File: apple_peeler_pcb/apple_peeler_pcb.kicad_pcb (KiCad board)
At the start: 2 copper layers, 130 parts, among them J1 BM03B-SRSS-TB, J2 BM03B-SRSS-TB, J3 HYC10-HDMIA19-600B, J4 HYC10-HDMIA19-600B, J5 USB_C_Receptacle_USB2.0_16P, Q1 2N7002, Q10 2N7002, Q11 2N7002, Q12 2N7002, Q13 2N7002, Q14 AO3401A, Q15 2N7002, Q16 AO3401A, Q17 2N7002, Q18 2N7002, Q2 2N7002, Q3 2N7002, Q4 2N7002, Q5 2N7002, Q6 2N7002, Q7 2N7002, Q8 2N7002, Q9 2N7002, SW1 SPST BTN, SW2 SPST BTN, SW3 SPST BTN, U1 W25Q16JVSS, U2 RP2040, U3 4066, U4 TPS562242, Y1 12MHz

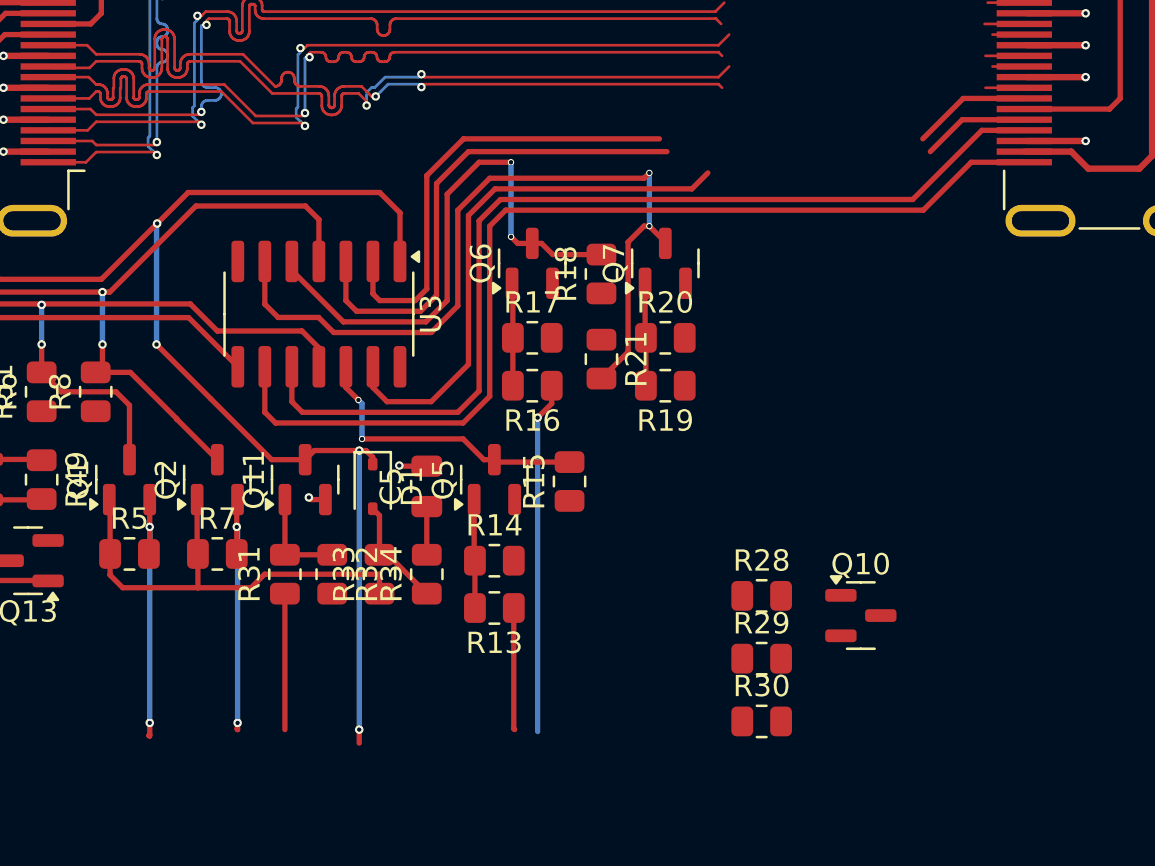
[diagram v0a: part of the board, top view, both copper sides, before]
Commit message: passthrough switch level shifters
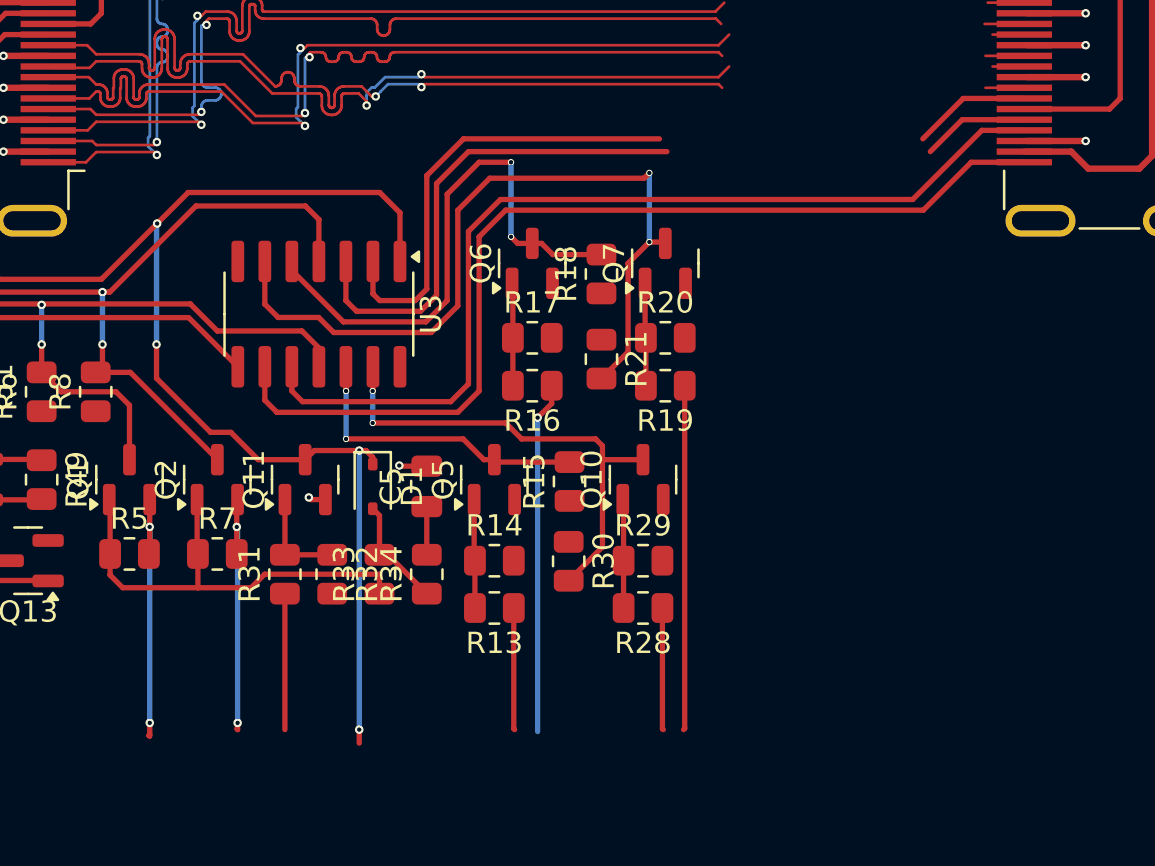
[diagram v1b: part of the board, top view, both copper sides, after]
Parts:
- moved Q10 12.1 mm to (191.5, 125.4), turned to 90 degrees
- moved R30 11.8 mm to (188.0, 129.2), turned to -90 degrees
- moved R29 7.23 mm to (191.5, 129.2)
- moved R28 5.60 mm to (191.5, 131.4), turned to 180 degrees
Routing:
- net /HDMI passthrough/HPD_ARC_BRIDGE: track 0.00 -> 16.2 mm
- net /HDMI passthrough/CEC_BRIDGE: track 0.00 -> 5.73 mm
- net Net-(Q10-G): track 0.00 -> 5.11 mm
- net /HDMI passthrough/Pullup level shifter3/OUT_5V: track 25.5 -> 22.8 mm, vias 0 -> 2
- net /HDMI passthrough/Bidir level shifter2/L_5V: track 46.4 -> 45.2 mm
- net /HDMI passthrough/HDMI connectors/HPD_SINK: track 47.8 -> 46.6 mm
- net /HDMI passthrough/CEC interface/CEC_LINE: track 70.0 -> 70.9 mm

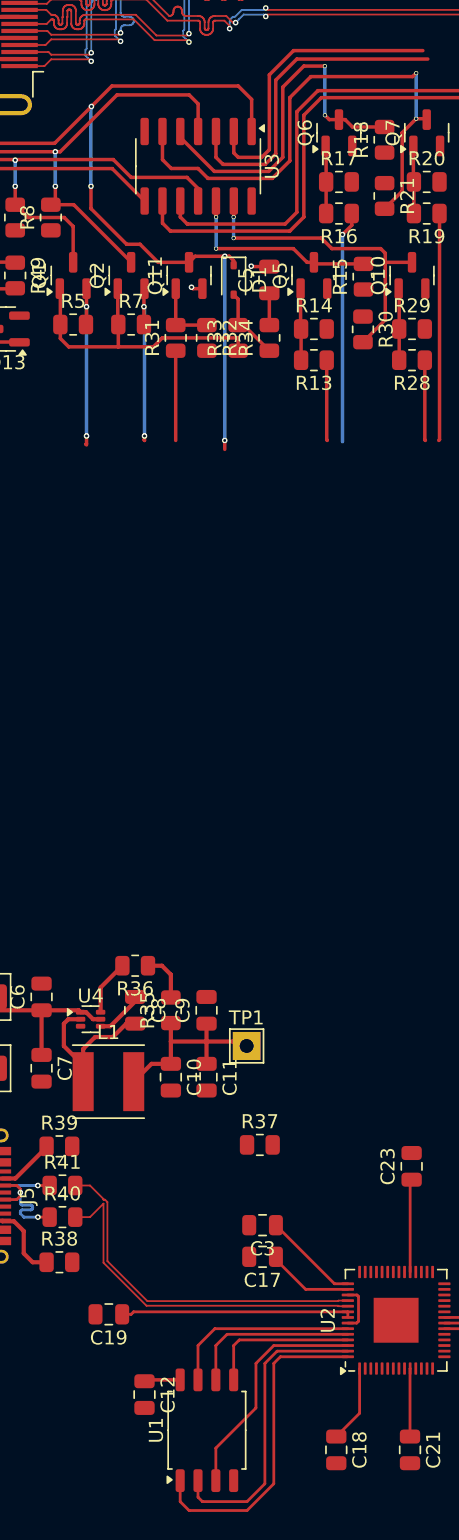
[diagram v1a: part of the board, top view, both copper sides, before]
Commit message: make space for bypass cap near switch chip
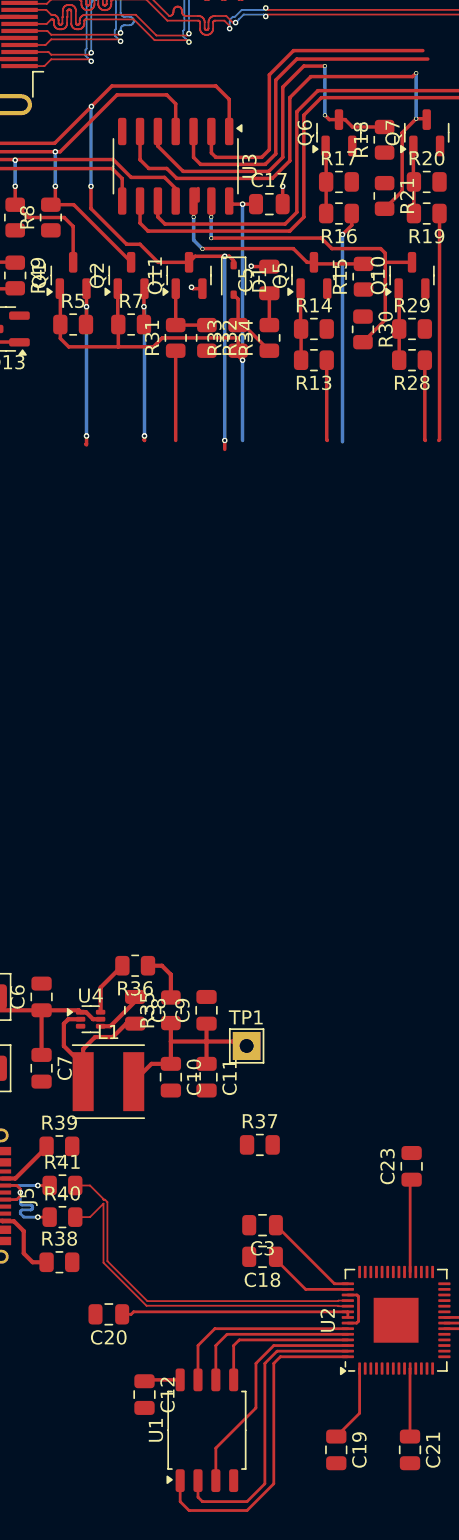
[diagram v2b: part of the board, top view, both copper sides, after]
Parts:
- added C17: 2.2μF, Capacitor_SMD:C_0805_2012Metric, F.Cu at (181.3, 120.3)
- moved U3 1.60 mm to (174.6, 117.6)
- renumbered C17 to C18, C18 to C19, C19 to C20
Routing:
- net +3.3V: track 88.7 -> 108.3 mm, vias 0 -> 2
- net /HDMI passthrough/Bidir level shifter/L_5V: track 46.1 -> 43.6 mm
- net /HDMI passthrough/HDMI connectors/HPD_SINK: track 46.6 -> 48.2 mm
- net /HDMI passthrough/CEC interface/CEC_LINE: track 70.9 -> 69.3 mm
- net /HDMI passthrough/Bidir level shifter2/L_5V: track 45.2 -> 46.8 mm
- net /HDMI passthrough/CEC interface1/CEC_LINE: track 26.9 -> 28.5 mm
- net /HDMI passthrough/Pullup level shifter2/OUT_5V: track 37.7 -> 39.3 mm
- net /HDMI passthrough/Bidir level shifter3/L_5V: track 28.4 -> 30.0 mm
- net /HDMI passthrough/Bidir level shifter1/L_5V: track 46.9 -> 45.3 mm
- net /HDMI passthrough/Pullup level shifter3/OUT_5V: track 22.8 -> 24.4 mm
- net /HDMI passthrough/Pullup level shifter1/OUT_5V: track 25.9 -> 27.4 mm
- net GND: track 29.7 -> 30.9 mm, vias 14 -> 15
- net /HDMI passthrough/Pullup level shifter/OUT_5V: track 14.3 -> 15.4 mm
- net /HDMI passthrough/HDMI connectors/HPD_SRC: track 45.3 -> 44.7 mm

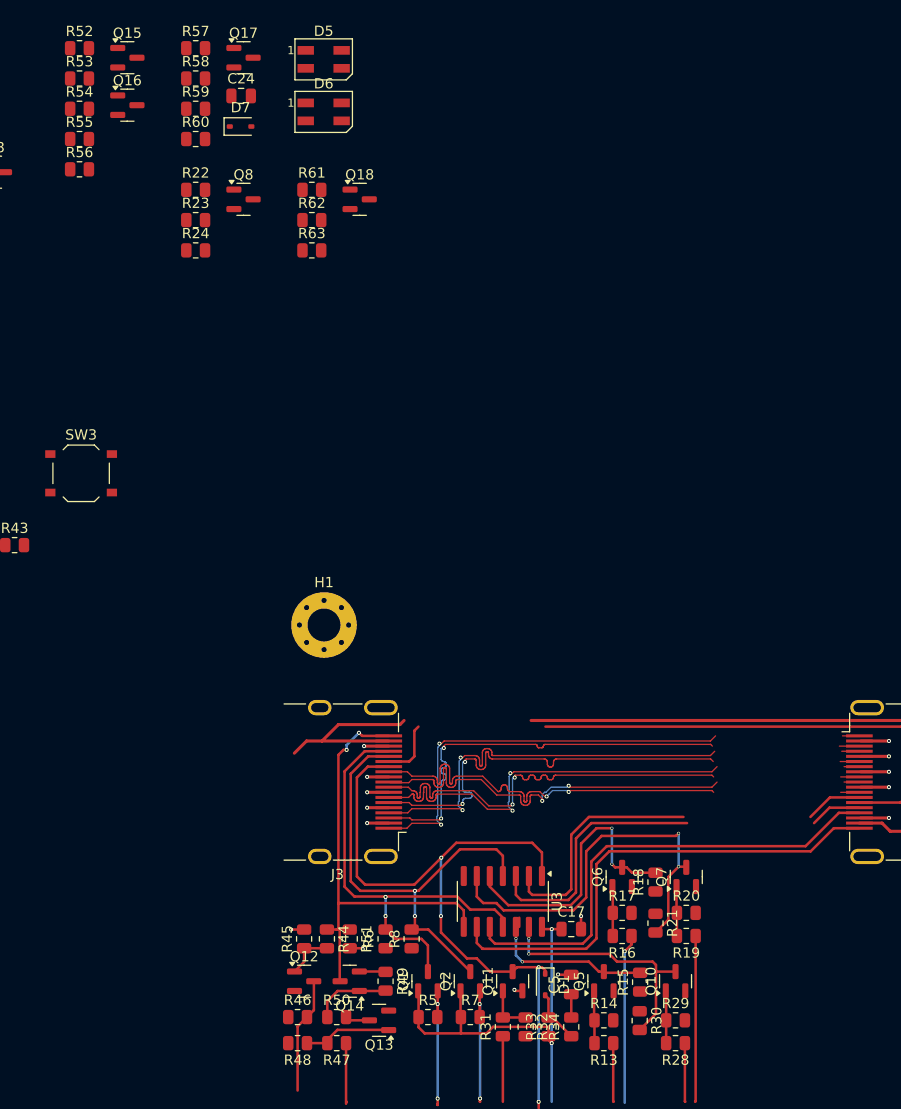
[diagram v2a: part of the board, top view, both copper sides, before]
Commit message: route HPD B
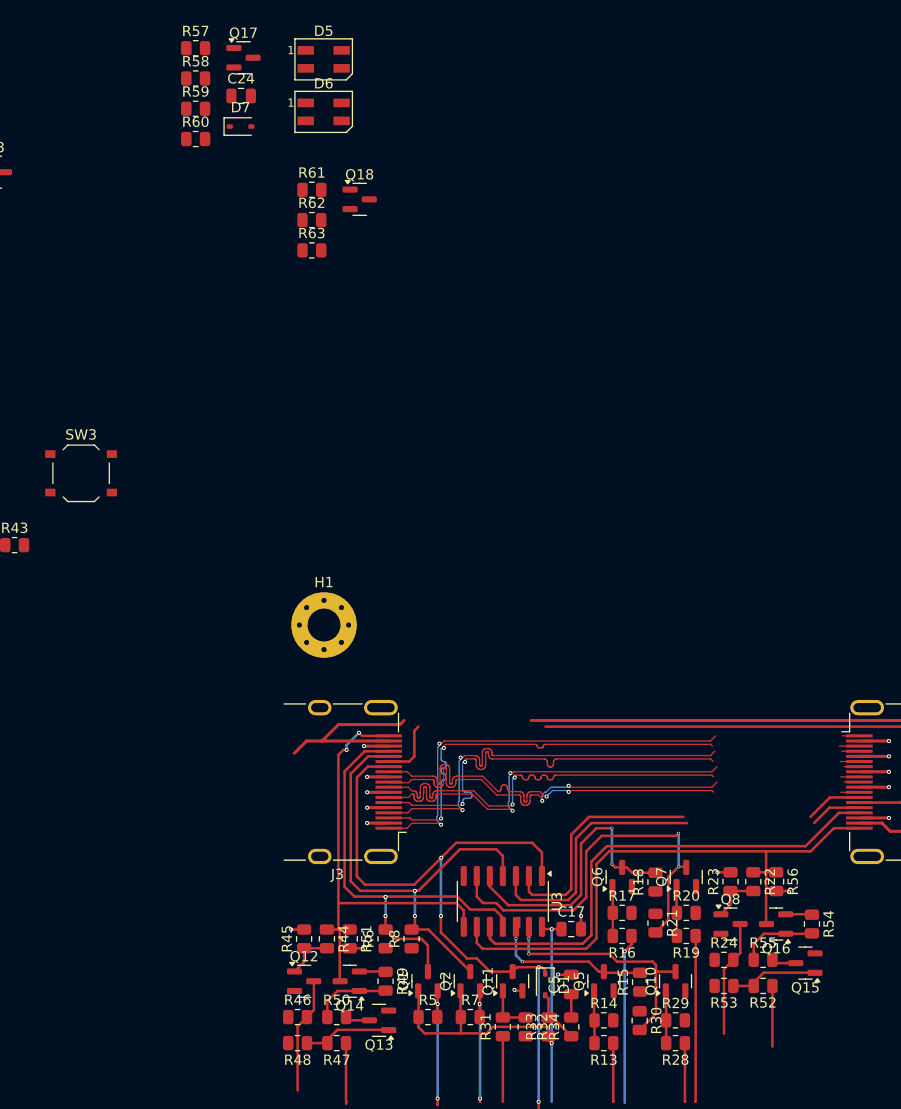
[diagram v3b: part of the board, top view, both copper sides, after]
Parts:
- moved R52 113.1 mm to (200.0, 125.9), turned to 180 degrees
- moved Q15 110.2 mm to (204.1, 123.6), turned to 180 degrees
- moved R53 108.5 mm to (196.2, 125.9), turned to 180 degrees
- moved R54 106.8 mm to (204.7, 119.8), turned to -90 degrees
- moved R55 104.1 mm to (200.0, 123.3)
- moved Q16 101.8 mm to (201.3, 119.8), turned to 180 degrees
- moved R56 97.1 mm to (201.3, 115.7), turned to -90 degrees
- moved R22 86.6 mm to (199.0, 115.7), turned to -90 degrees
- moved R24 86.2 mm to (196.2, 123.3)
- moved Q8 85.1 mm to (196.8, 119.8)
- moved R23 82.9 mm to (196.8, 115.7), turned to 90 degrees
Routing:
- net /HDMI passthrough/HPD_SINK_MON: track 0.00 -> 11.3 mm
- net /HDMI passthrough/HDMI connectors/HPD_SINK: track 48.2 -> 57.5 mm
- net Net-(Q15-G): track 0.00 -> 8.69 mm
- net Net-(Q16-G): track 0.00 -> 7.65 mm
- net /HDMI passthrough/HPD_SINK_ASSERT: track 0.00 -> 5.91 mm
- net Net-(Q8-G): track 0.00 -> 4.88 mm
- net GND: track 30.9 -> 33.9 mm, vias 15 -> 17
- net +5V: track 19.0 -> 21.6 mm
- net Net-(Q15-D): track 0.00 -> 2.41 mm

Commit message: half-a-cec
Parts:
- moved C24 121.4 mm to (217.8, 139.2)
- moved R59 121.4 mm to (213.4, 140.4)
- moved D7 121.4 mm to (217.8, 142.2)
- moved R58 121.4 mm to (213.4, 137.5)
- moved R60 121.4 mm to (213.4, 143.4)
- moved R9 116.3 mm to (208.6, 121.6)
- moved R57 112.8 mm to (215.6, 122.2), turned to 90 degrees
- moved R11 110.4 mm to (212.4, 121.6)
- moved Q3 109.9 mm to (208.6, 118.1), turned to 90 degrees
- moved R10 106.6 mm to (203.2, 115.9), turned to 90 degrees
- moved Q17 106.3 mm to (216.2, 118.1), turned to 90 degrees
- moved Q4 104.1 mm to (212.4, 118.1), turned to 90 degrees
- moved R12 99.9 mm to (205.4, 115.9), turned to 90 degrees
- moved Q18 28.5 mm to (173.0, 74.9), turned to 90 degrees
- moved Q12 0.64 mm to (155.9, 125.4)
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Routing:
- net /HDMI passthrough/CEC interface1/CEC_LINE: track 28.5 -> 45.9 mm, vias 0 -> 2
- net /HDMI passthrough/SCL_SINK_3V3: track 0.00 -> 15.0 mm, vias 0 -> 1
- net /HDMI passthrough/SDA_SINK_3V3: track 0.00 -> 14.7 mm, vias 0 -> 1
- net /HDMI passthrough/Bidir level shifter3/L_5V: track 30.0 -> 43.0 mm, vias 0 -> 2
- net +3.3V: track 108.3 -> 119.7 mm
- net /HDMI passthrough/Bidir level shifter2/L_5V: track 46.8 -> 56.9 mm, vias 0 -> 2
- net Net-(Q17-G): track 0.00 -> 2.57 mm

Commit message: final level shifter
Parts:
- moved D7 19.9 mm to (218.1, 122.2), turned to -90 degrees
- moved R60 17.5 mm to (215.6, 126.0), turned to -90 degrees
- moved R59 15.1 mm to (218.1, 126.0), turned to 90 degrees
- moved C24 14.0 mm to (213.0, 126.0), turned to 90 degrees
- moved R58 11.8 mm to (210.5, 126.0), turned to -90 degrees
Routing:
- net /HDMI passthrough/CEC_SINK_PULLDOWN: track 0.00 -> 10.5 mm, vias 0 -> 1
- net +3.3V: track 119.7 -> 129.3 mm
- net Net-(Q17-G): track 2.57 -> 9.25 mm
- net /HDMI passthrough/CEC interface1/CEC_LINE: track 45.9 -> 51.0 mm
- net Net-(D7-A): track 0.00 -> 4.39 mm

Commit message: sane names for subsheets
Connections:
- net /HDMI passthrough/Bidir level shifter/L_5V renamed /HDMI passthrough/Bidir level shifter 1/L_5V
- net /HDMI passthrough/Bidir level shifter1/L_5V renamed /HDMI passthrough/Bidir level shifter 2/L_5V
- net /HDMI passthrough/Bidir level shifter2/L_5V renamed /HDMI passthrough/Bidir level shifter 3/L_5V
- net /HDMI passthrough/Bidir level shifter3/L_5V renamed /HDMI passthrough/Bidir level shifter 4/L_5V
- net /HDMI passthrough/CEC interface/CEC_LINE renamed /HDMI passthrough/CEC interface 1/CEC_LINE
- net /HDMI passthrough/CEC interface1/CEC_LINE renamed /HDMI passthrough/CEC interface 2/CEC_LINE
- net /HDMI passthrough/Pullup level shifter/OUT_5V renamed /HDMI passthrough/Pullup level shifter 1/OUT_5V
- net /HDMI passthrough/Pullup level shifter1/OUT_5V renamed /HDMI passthrough/Pullup level shifter 2/OUT_5V
- net /HDMI passthrough/Pullup level shifter2/OUT_5V renamed /HDMI passthrough/Pullup level shifter 3/OUT_5V
- net /HDMI passthrough/Pullup level shifter3/OUT_5V renamed /HDMI passthrough/Pullup level shifter 4/OUT_5V
